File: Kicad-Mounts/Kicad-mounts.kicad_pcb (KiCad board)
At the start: 2 copper layers, 25 x 35.6 mm, 10 parts, among them P1 CONN_10, P2 CONN_10, P3 CONN_6X2, P6 CONN_3, U2 TPS77033

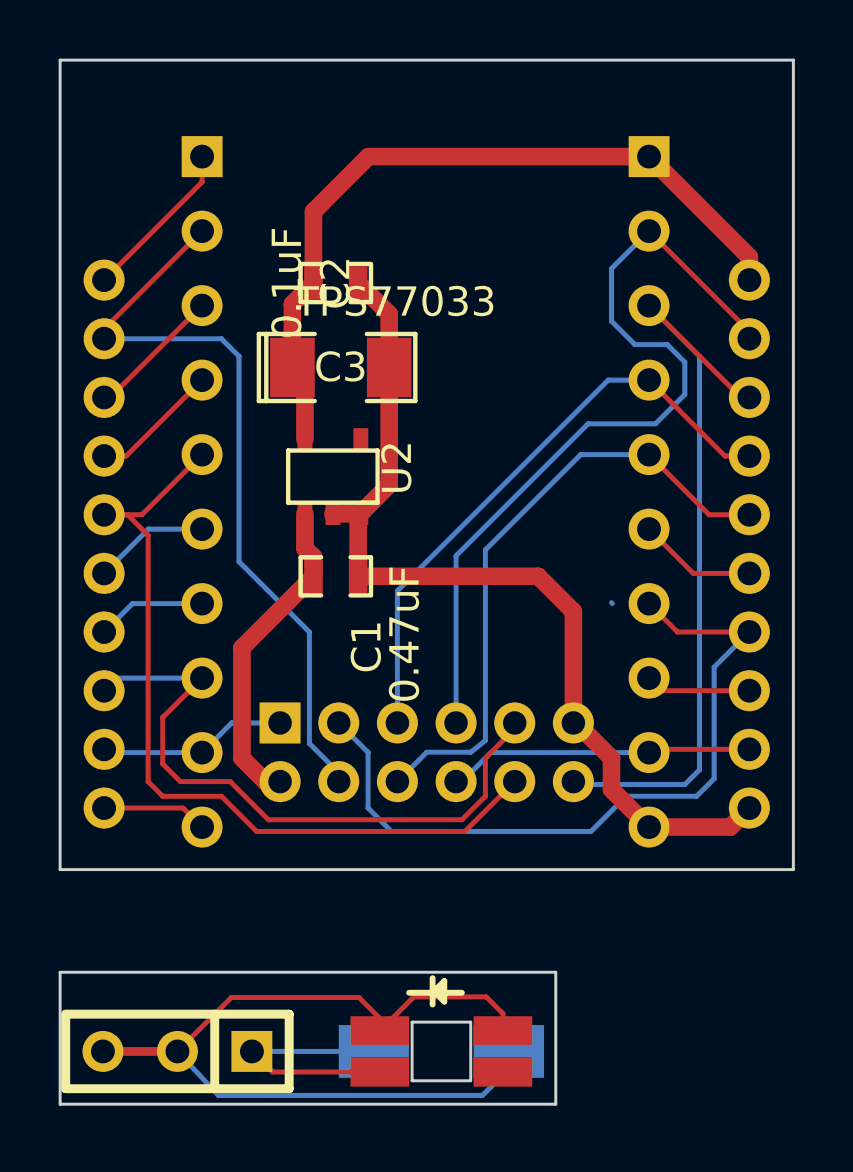
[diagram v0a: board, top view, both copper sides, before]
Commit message: Change RTS pin to Association pin for possible monitoring. Update README
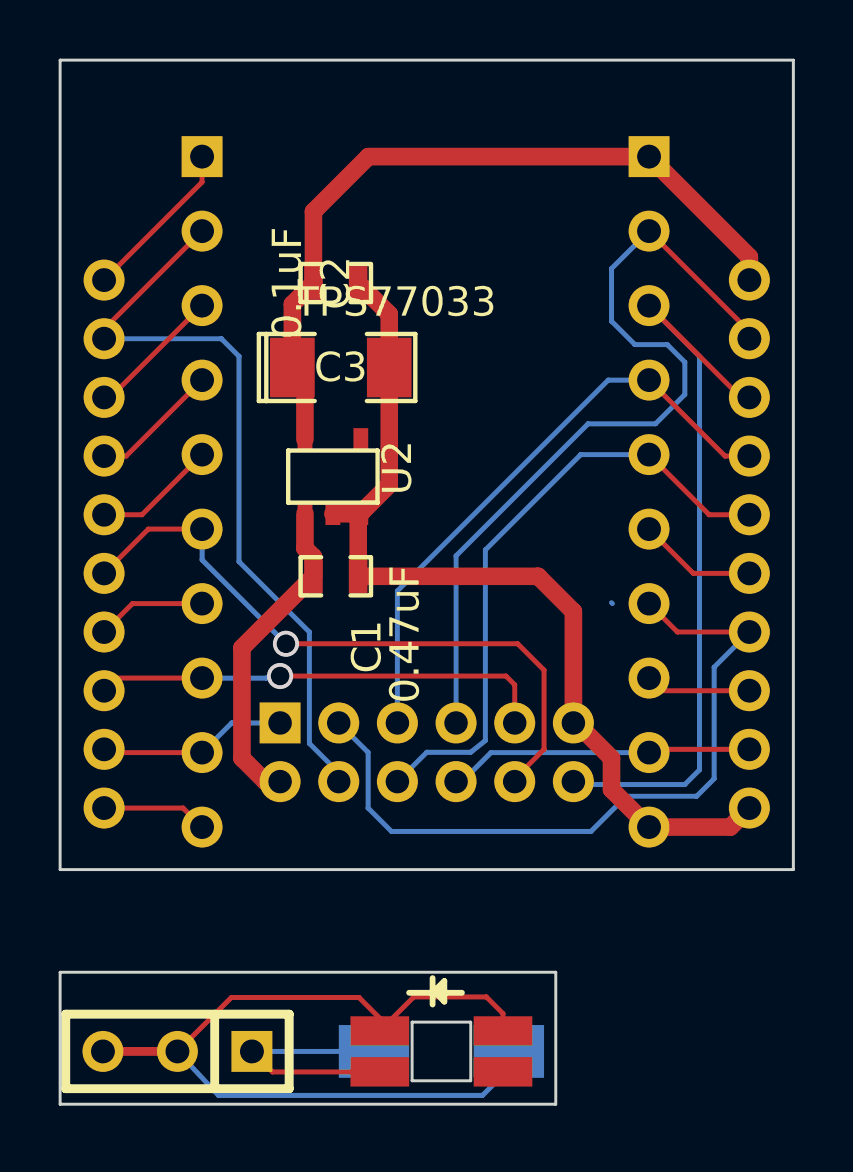
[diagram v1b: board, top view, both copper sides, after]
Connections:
- P2 pad 6: Net-(P2-Pad6) -> /Association
- P3 pad 10: /RTS -> /Association
- XB1 pad 15: Net-(P2-Pad6) -> /Association
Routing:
- net /RTS: track 28.3 -> 4.19 mm
- net /Association: track 0.00 -> 22.4 mm, vias 0 -> 1
- net /On/Sleep: track 23.3 -> 15.7 mm, vias 0 -> 1
- net Net-(P2-Pad6): track 3.97 -> 0.00 mm

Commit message: Major new version of the PCBs for next stage of production run.
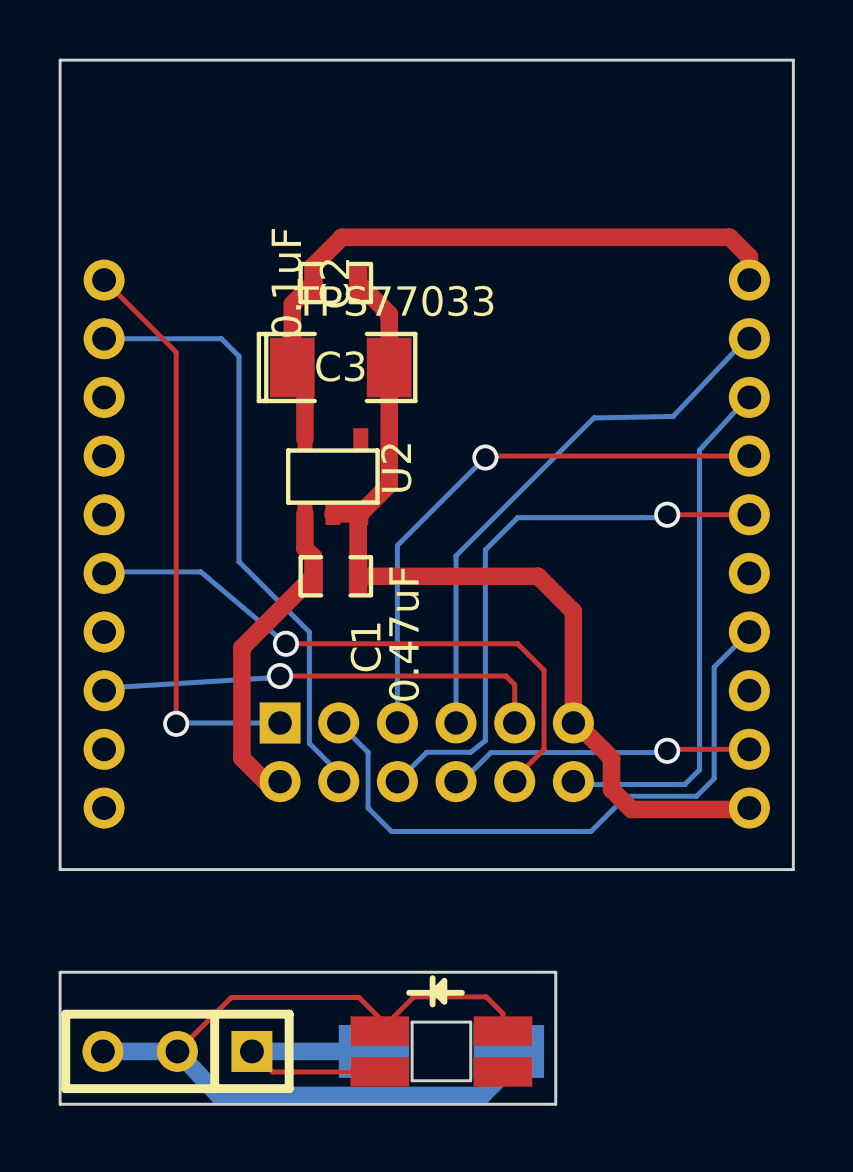
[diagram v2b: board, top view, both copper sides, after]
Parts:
- removed P1, P2: CONN_10, Connect:SIL-10
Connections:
- P3 pad 1: /CTS -> /Commissioning
- XB1 pad 20: Net-(P2-Pad1) -> /Commissioning
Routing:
- net /Commissioning: track 0.00 -> 19.7 mm, vias 0 -> 1
- net /Rx: track 28.6 -> 19.0 mm
- net /Tx: track 25.8 -> 18.1 mm
- net /CTS: track 6.74 -> 0.16 mm
- net Net-(P2-Pad1): track 5.59 -> 0.00 mm
- net /VBatt: track 26.1 -> 21.4 mm
- net Net-(XB1-Pad18): track 4.64 -> 0.21 mm
- net Net-(XB1-Pad17): track 4.41 -> 0.00 mm
- net Net-(XB1-Pad8): track 4.21 -> 0.00 mm
- net /RTS: track 4.19 -> 0.00 mm
- net Net-(XB1-Pad6): track 4.05 -> 0.00 mm
- net /Bootloader: track 25.7 -> 21.9 mm
- net Net-(XB1-Pad14): track 3.74 -> 0.00 mm
- net Net-(XB1-Pad11): track 3.61 -> 0.00 mm
- net /V3: track 26.1 -> 22.7 mm
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
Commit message: Update to Kicad PCB files to slightly adjust components and footprints to accomodate purchased materials.
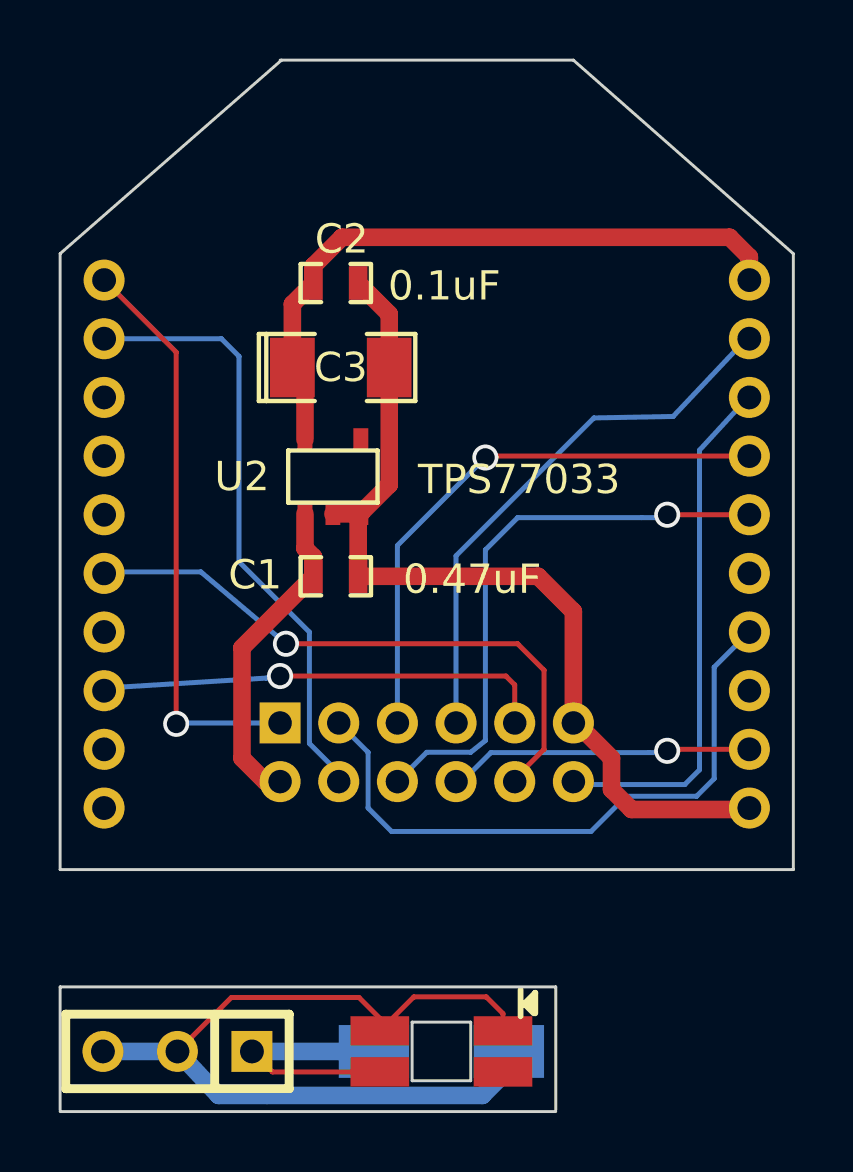
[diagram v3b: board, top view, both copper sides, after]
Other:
- board size 25 x 35.6 mm -> 25 x 35.8 mm
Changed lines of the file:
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@@
-(kicad_pcb (version 4) (host pcbnew 4.0.2-4+6225~38~ubuntu14.04.1-stable)
+(kicad_pcb (version 4) (host pcbnew 4.1.0-alpha+201605180746+6813~44~ubuntu14.04.1-product)
   (general
     (links 24)
     (no_connects 0)
-    (area 167.949999 90.349999 193.050001 126.050001)
+    (area 167.693499 90.349999 193.306501 128.508676)
     (thickness 1.6)
-    (drawings 20)
+    (drawings 19)
     (tracks 134)
     (zones 0)
@@
     (0 F.Cu signal)
     (31 B.Cu signal)
-    (32 B.Adhes user)
-    (33 F.Adhes user)
-    (34 B.Paste user)
-    (35 F.Paste user)
+    (32 B.Adhes user hide)
+    (33 F.Adhes user hide)
+    (34 B.Paste user hide)
+    (35 F.Paste user hide)
     (36 B.SilkS user)
-    (37 F.SilkS user hide)
-    (38 B.Mask user)
-    (39 F.Mask user)
-    (40 Dwgs.User user)
-    (41 Cmts.User user)
-    (42 Eco1.User user)
-    (43 Eco2.User user)
+    (37 F.SilkS user)
+    (38 B.Mask user hide)
+    (39 F.Mask user hide)
+    (40 Dwgs.User user hide)
+    (41 Cmts.User user hide)
+    (42 Eco1.User user hide)
+    (43 Eco2.User user hide)
     (44 Edge.Cuts user)
-    (45 Margin user)
-    (46 B.CrtYd user)
-    (47 F.CrtYd user)
-    (48 B.Fab user)
-    (49 F.Fab user)
+    (45 Margin user hide)
+    (46 B.CrtYd user hide)
+    (47 F.CrtYd user hide)
+    (48 B.Fab user hide)
+    (49 F.Fab user hide)
   )
   (setup
@@
       (hpglpenspeed 20)
       (hpglpendiameter 15)
-      (hpglpenoverlay 2)
       (psnegative false)
       (psa4output false)
@@
     (at 177.4 108)
     (attr smd)
-    (fp_text reference C1 (at 1.06 2.4 90) (layer F.SilkS)
-      (effects (font (size 1 1) (thickness 0.15)))
-    )
-    (fp_text value 0.47uF (at 2.36 1.98 90) (layer F.SilkS)
+    (fp_text reference C1 (at -2.75 -0.05 180) (layer F.SilkS)
+      (effects (font (size 1 1) (thickness 0.15)))
+    )
+    (fp_text value 0.47uF (at 4.65 0.1 180) (layer F.SilkS)
       (effects (font (size 1 1) (thickness 0.15)))
     )
@@
     (at 177.4 98)
     (attr smd)
-    (fp_text reference C2 (at 0 0 90) (layer F.SilkS)
-      (effects (font (size 1 1) (thickness 0.15)))
-    )
-    (fp_text value 0.1uF (at -1.651 0 90) (layer F.SilkS)
+    (fp_text reference C2 (at 0.2 -1.5 180) (layer F.SilkS)
+      (effects (font (size 1 1) (thickness 0.15)))
+    )
+    (fp_text value 0.1uF (at 3.7 0.1 180) (layer F.SilkS)
       (effects (font (size 1 1) (thickness 0.15)))
     )
@@
     (at 177.3 104.6)
     (attr smd)
-    (fp_text reference U2 (at 2.19964 -0.29972 90) (layer F.SilkS)
-      (effects (font (size 1 1) (thickness 0.15)))
-    )
-    (fp_text value TPS77033 (at 2.13 -5.95) (layer F.SilkS)
+    (fp_text reference U2 (at -3.1 0 180) (layer F.SilkS)
+      (effects (font (size 1 1) (thickness 0.15)))
+    )
+    (fp_text value TPS77033 (at 6.35 0.1) (layer F.SilkS)
       (effects (font (size 1 1) (thickness 0.15)))
     )
@@
     )
   )
-  (gr_line (start 168 121.5) (end 168 126) (angle 90) (layer Edge.Cuts) (width 0.1))
-  (gr_line (start 168 121.5) (end 184.9 121.5) (angle 90) (layer Edge.Cuts) (width 0.1))
-  (gr_line (start 184.9 121.5) (end 184.9 126) (angle 90) (layer Edge.Cuts) (width 0.1))
+  (gr_line (start 185.5 90.4) (end 193 97) (angle 90) (layer Edge.Cuts) (width 0.1))
+  (gr_line (start 175.55 90.4) (end 168 97) (angle 90) (layer Edge.Cuts) (width 0.1))
+  (gr_line (start 168 122) (end 168 126.2) (angle 90) (layer Edge.Cuts) (width 0.1))
+  (gr_line (start 168 122) (end 184.9 122) (angle 90) (layer Edge.Cuts) (width 0.1))
+  (gr_line (start 184.9 122) (end 184.9 126.2) (angle 90) (layer Edge.Cuts) (width 0.1))
   (gr_line (start 182 123.2) (end 182 125.2) (angle 90) (layer Edge.Cuts) (width 0.1))
   (gr_line (start 180 123.2) (end 180 125.2) (angle 90) (layer Edge.Cuts) (width 0.1))
   (gr_line (start 180 125.2) (end 182 125.2) (angle 90) (layer Edge.Cuts) (width 0.1))
   (gr_line (start 180 123.2) (end 182 123.2) (angle 90) (layer Edge.Cuts) (width 0.1))
-  (gr_line (start 181 122) (end 181 122.3) (angle 90) (layer F.SilkS) (width 0.2))
-  (gr_line (start 180.7 121.7) (end 180.7 122.6) (angle 90) (layer F.SilkS) (width 0.2))
-  (gr_line (start 181.1 122.2) (end 181.7 122.2) (angle 90) (layer F.SilkS) (width 0.2))
-  (gr_line (start 180.8 122.2) (end 180.7 122.2) (angle 90) (layer F.SilkS) (width 0.2))
-  (gr_line (start 181.1 122.5) (end 180.8 122.2) (angle 90) (layer F.SilkS) (width 0.2))
-  (gr_line (start 181.1 121.8) (end 181.1 122.5) (angle 90) (layer F.SilkS) (width 0.2))
-  (gr_line (start 180.7 122.2) (end 181.1 121.8) (angle 90) (layer F.SilkS) (width 0.2))
-  (gr_line (start 179.9 122.2) (end 180.7 122.2) (angle 90) (layer F.SilkS) (width 0.2))
-  (gr_line (start 168 90.4) (end 193 90.4) (angle 90) (layer Edge.Cuts) (width 0.1))
-  (gr_line (start 193 118) (end 193 90.4) (angle 90) (layer Edge.Cuts) (width 0.1))
-  (gr_line (start 168 126) (end 184.9 126) (angle 90) (layer Edge.Cuts) (width 0.1))
+  (gr_line (start 184.05 122.45) (end 184.05 122.75) (angle 90) (layer F.SilkS) (width 0.2))
+  (gr_line (start 183.7 122.1) (end 183.7 123) (angle 90) (layer F.SilkS) (width 0.2))
+  (gr_line (start 184.15 122.9) (end 183.85 122.6) (angle 90) (layer F.SilkS) (width 0.2))
+  (gr_line (start 184.2 122.2) (end 184.2 122.9) (angle 90) (layer F.SilkS) (width 0.2))
+  (gr_line (start 183.8 122.6) (end 184.2 122.2) (angle 90) (layer F.SilkS) (width 0.2))
+  (gr_line (start 175.5 90.4) (end 185.5 90.4) (angle 90) (layer Edge.Cuts) (width 0.1))
+  (gr_line (start 193 118) (end 193 97) (angle 90) (layer Edge.Cuts) (width 0.1))
+  (gr_line (start 168 126.25) (end 184.9 126.25) (angle 90) (layer Edge.Cuts) (width 0.1))
   (gr_line (start 168 118) (end 193 118) (angle 90) (layer Edge.Cuts) (width 0.1))
-  (gr_line (start 168 118) (end 168 90.4) (angle 90) (layer Edge.Cuts) (width 0.1))
+  (gr_line (start 168 118) (end 168 97) (angle 90) (layer Edge.Cuts) (width 0.1))
   (segment (start 172 124.2) (end 169.46 124.2) (width 0.6) (layer B.Cu) (net 1))
   (segment (start 183.1 122.91) (end 182.53 122.34) (width 0.17) (layer F.Cu) (net 1))
@@
   (segment (start 191.50126 103.9) (end 191.50074 103.89948) (width 0.17) (layer B.Cu) (net 6))
   (segment (start 191.50074 105.901) (end 188.401 105.901) (width 0.17) (layer F.Cu) (net 7))
+  (segment (start 188.401 105.901) (end 188.402 105.9) (width 0.17) (layer F.Cu) (net 7))
+  (segment (start 188.402 105.9) (end 188.7 105.9) (width 0.17) (layer F.Cu) (net 7))
+  (via (at 188.7 105.9) (size 0.889) (drill 0.635) (layers F.Cu B.Cu) (net 7))
+  (segment (start 188.7 105.9) (end 188.6 106) (width 0.17) (layer B.Cu) (net 7))
+  (segment (start 188.6 106) (end 187.83 106) (width 0.17) (layer B.Cu) (net 7))
+  (segment (start 187.83 106) (end 183.6 106) (width 0.17) (layer B.Cu) (net 7))
+  (segment (start 183.6 106) (end 182.5 107.1) (width 0.17) (layer B.Cu) (net 7))
+  (segment (start 180.5 114) (end 179.5 115) (width 0.17) (layer B.Cu) (net 7))
+  (segment (start 182 114) (end 180.5 114) (width 0.17) (layer B.Cu) (net 7))
+  (segment (start 182.5 113.6) (end 182 114) (width 0.17) (layer B.Cu) (net 7))
   (segment (start 182.5 107.1) (end 182.5 113.6) (width 0.17) (layer B.Cu) (net 7))
-  (segment (start 182.5 113.6) (end 182 114) (width 0.17) (layer B.Cu) (net 7))
-  (segment (start 182 114) (end 180.5 114) (width 0.17) (layer B.Cu) (net 7))
-  (segment (start 180.5 114) (end 179.5 115) (width 0.17) (layer B.Cu) (net 7))
-  (segment (start 183.6 106) (end 182.5 107.1) (width 0.17) (layer B.Cu) (net 7))
-  (segment (start 187.83 106) (end 183.6 106) (width 0.17) (layer B.Cu) (net 7))
-  (segment (start 188.6 106) (end 187.83 106) (width 0.17) (layer B.Cu) (net 7))
-  (segment (start 188.7 105.9) (end 188.6 106) (width 0.17) (layer B.Cu) (net 7))
-  (via (at 188.7 105.9) (size 0.889) (drill 0.635) (layers F.Cu B.Cu) (net 7))
-  (segment (start 188.402 105.9) (end 188.7 105.9) (width 0.17) (layer F.Cu) (net 7))
-  (segment (start 188.401 105.901) (end 188.402 105.9) (width 0.17) (layer F.Cu) (net 7))
   (segment (start 191.70104 109.89896) (end 191.50074 109.89896) (width 0.17) (layer F.Cu) (net 8))
   (segment (start 177.5 113) (end 178.5 114) (width 0.17) (layer B.Cu) (net 8))
@@
   (segment (start 175.7 110.3) (end 172.8 107.85) (width 0.17) (layer B.Cu) (net 17))
   (segment (start 172.8 107.85) (end 169.45 107.85) (width 0.17) (layer B.Cu) (net 17))
-  (segment (start 175.5 113) (end 171.988 113) (width 0.17) (layer B.Cu) (net 18) (status 400000))
-  (segment (start 171.958 100.35874) (end 169.49926 97.9) (width 0.17) (layer F.Cu) (net 18) (status 800000))
+  (segment (start 175.5 113) (end 171.988 113) (width 0.17) (layer B.Cu) (net 18))
+  (segment (start 171.958 100.35874) (end 169.49926 97.9) (width 0.17) (layer F.Cu) (net 18))
   (segment (start 171.958 113.03) (end 171.958 100.35874) (width 0.17) (layer F.Cu) (net 18))
   (segment (start 171.958 113.03) (end 171.958 113.03) (width 0.17) (layer F.Cu) (net 18))
